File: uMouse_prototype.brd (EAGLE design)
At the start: 90 x 100 mm, 76 parts, among them IC1 LM1117IMPX-5.0, IC2 LM1117IMPX-5.0

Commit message: gotowa, czeka na uwagi Tomka i Kuby
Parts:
- added C27: 100nF 6.3V, rcl:C0805K
- added U$2: (no value), Nordic_nRF:RESC0805_L
- moved 7V4-ON 5.24 mm to (4.45, 57.1), turned to 90 degrees
- moved R1 5.24 mm to (9.53, 57.1), turned to 0 degrees
- moved C6 3.81 mm to (41.9, 73.0)
- moved C7 3.81 mm to (41.9, 76.2)
- moved Q3 2.54 mm to (62.9, 81.3)
- moved C14 1.91 mm to (6.99, 74.9)
- moved C15 1.91 mm to (6.99, 71.8)
- moved IR3 0.38 mm to (60.1, 89.5)
- turned C13 to 90 degrees
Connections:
- removed net AGND: C18.2, C19.2, C20.2, C21.2, C22.2, PT1.K, PT2.K, PT3.K, PT4.K, PT5.K, R19.1, R22.1, U$5.AGND
- removed net N$25: U$5.PA15
- new net N$22: U$2.2, U$5.AVDD
- net 7.4V/VBAT: now also C25.1, C26.1, U$3.5
- net GND: now also C18.2, C19.2, C20.2, C21.2, C22.2, C27.2, PT1.K, PT2.K, PT3.K, PT4.K, PT5.K, R19.1, R22.1, U$5.AGND, U$5.GND_1, U$5.GND_2, U$5.GND_3, U$5.GND_4, U$5.GND_5
- net LEFT-ENC-A: now also JP2.3, U$5.PA0; no longer JP1.1, U$5.PC10
- net LEFT-ENC-B: now also JP2.1, U$5.PA1; no longer JP1.3, U$5.PC12
- net LEFT-M-OUT1: now also JP2.2, U$3.6; no longer JP1.2, U$1.6
- net LEFT-M-OUT2: now also JP2.4, U$3.8; no longer JP1.4, U$1.8
- net LEFT-M-PWM1: now also U$3.3, U$5.PC8; no longer U$1.3, U$5.PB10, U$5.PC6
- net LEFT-M-PWM2: now also U$3.2, U$5.PC6; no longer U$1.2, U$5.PC7
- net RECEIVER_1: now also U$5.PA6; no longer U$5.PA0
- net RECEIVER_2: now also U$5.PA5; no longer U$5.PA1
- net RIGHT-ENC-A: now also JP1.3, U$5.PA9; no longer JP2.1, U$5.PA13
- net RIGHT-ENC-B: now also JP1.1, U$5.PA8; no longer JP2.3, U$5.PA14
- net RIGHT-M-OUT1: now also JP1.2, U$1.6; no longer JP2.2, U$3.6
- net RIGHT-M-OUT2: now also JP1.4, U$1.8; no longer JP2.4, U$3.8
- net RIGHT-M-PWM1: now also U$1.3, U$5.PC9; no longer U$3.3, U$5.PB3, U$5.PC8
- net RIGHT-M-PWM2: now also U$1.2, U$5.PC7; no longer U$3.2, U$5.PB4, U$5.PC9
- net VBAT: no longer C25.1, C26.1, U$3.5
- net VCC: now also C27.1, U$2.1
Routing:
- net VCC: track 0.00 -> 317.8 mm, vias 0 -> 6
- net 7.4V/VBAT: track 0.00 -> 110.1 mm
- net RECEIVER_3: track 0.00 -> 90.9 mm, vias 0 -> 1
- net LEFT-M-PWM1: track 0.00 -> 70.2 mm, vias 0 -> 3
- net LEFT-M-PWM2: track 0.00 -> 68.9 mm, vias 0 -> 3
- net RECEIVER_5: track 0.00 -> 63.3 mm
- net RECEIVER_1: track 0.00 -> 61.4 mm
- net SCL: track 0.00 -> 60.9 mm, vias 0 -> 1
- net SDA: track 0.00 -> 59.6 mm, vias 0 -> 1
- net RECEIVER_4: track 0.00 -> 57.6 mm, vias 0 -> 1
- net RECEIVER_2: track 0.00 -> 56.4 mm
- net RIGHT-M-PWM1: track 0.00 -> 47.9 mm, vias 0 -> 3
- net INT: track 0.00 -> 33.7 mm
- net RIGHT-ENC-B: track 0.00 -> 33.4 mm
- net RIGHT-ENC-A: track 0.00 -> 32.5 mm
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- added copper zone on layer 1, net GND

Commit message: ostatnie poprawki, plytka do enkoderow
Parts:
- added C28: 1uF 16V, rcl:C0805K
- added C29: 4.7uF 6.3V, rcl:C0805K
- added C30: 100nF 6.3V, rcl:C0805K
- added IC3: LM1117IMPX-5.0, lm1117:SOT223
- added JP3, JP4: (no value), pinhead:1X02
- added JP5: (no value), pinhead:1X06
- moved 7V4-ON 5.75 mm to (5.08, 62.9)
- moved R1 5.75 mm to (8.89, 62.9)
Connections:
- new net 5V: C29.1, C30.1, IC3.2, IC3.TAB, JP5.5
- new net EN: JP5.6
- new net RX-STM: JP5.3, U$5.PC5
- new net STATE: JP5.1
- new net TX-STM: JP5.2, U$5.PB10
- net 7.4V/VBAT: now also C28.1, IC3.3
- net GND: now also C28.2, C29.2, C30.2, IC3.1, JP5.4
- net LEFT-M-OUT1: now also JP4.1
- net LEFT-M-OUT2: now also JP4.2
- net RIGHT-M-OUT1: now also JP3.1
- net RIGHT-M-OUT2: now also JP3.2
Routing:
- net LEFT-M-OUT1: track 4.60 -> 45.1 mm, vias 0 -> 1
- net 7.4V/VBAT: track 110.1 -> 143.8 mm, vias 0 -> 2
- net RX-STM: track 0.00 -> 33.0 mm, vias 0 -> 1
- net 5V: track 0.00 -> 26.6 mm, vias 0 -> 2
- net RIGHT-M-OUT2: track 5.24 -> 23.0 mm, vias 0 -> 1
- net RIGHT-M-OUT1: track 5.61 -> 19.8 mm, vias 0 -> 1
- net TX-STM: track 0.00 -> 11.3 mm
- net LEFT-M-OUT2: track 4.60 -> 14.6 mm
- net N$1: track 3.08 -> 1.81 mm
- net INT: vias 0 -> 1

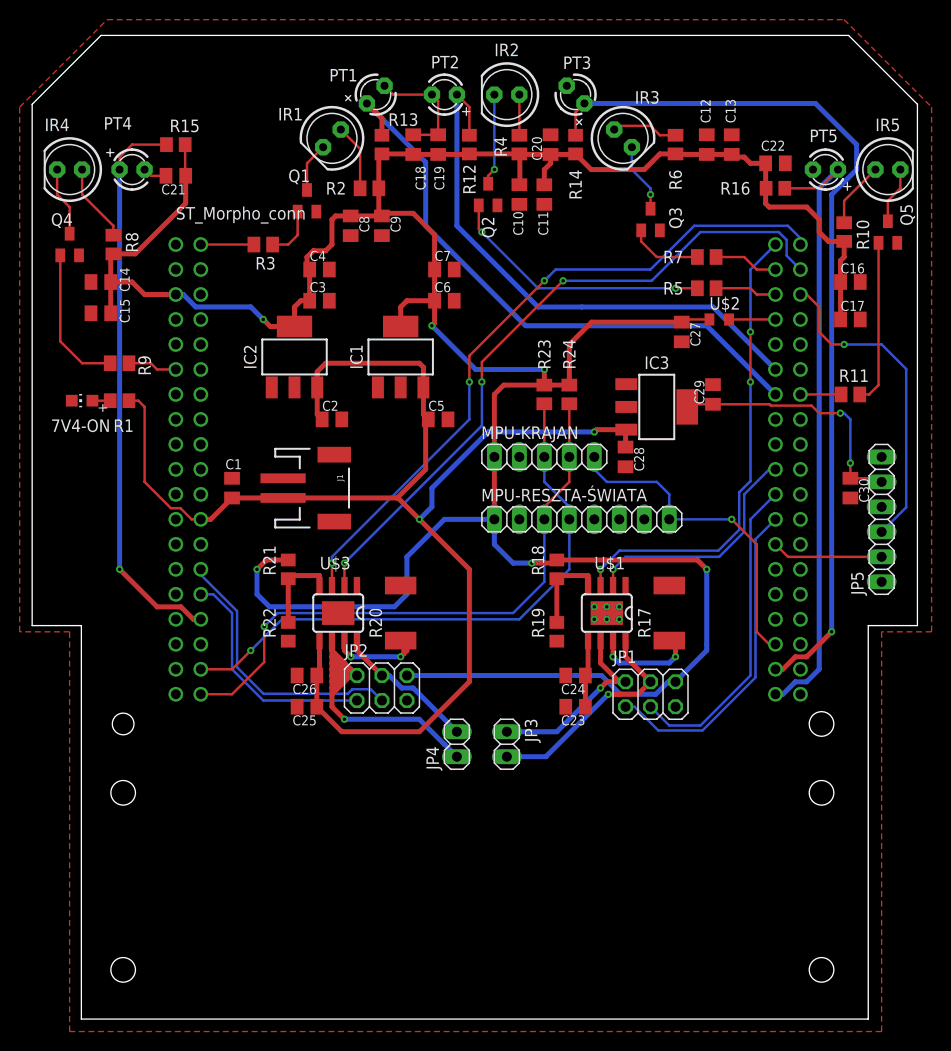
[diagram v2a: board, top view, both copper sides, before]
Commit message: poprawione i2c, dodane otwory pod holderki do ledów IR (tylko przy dwóch)
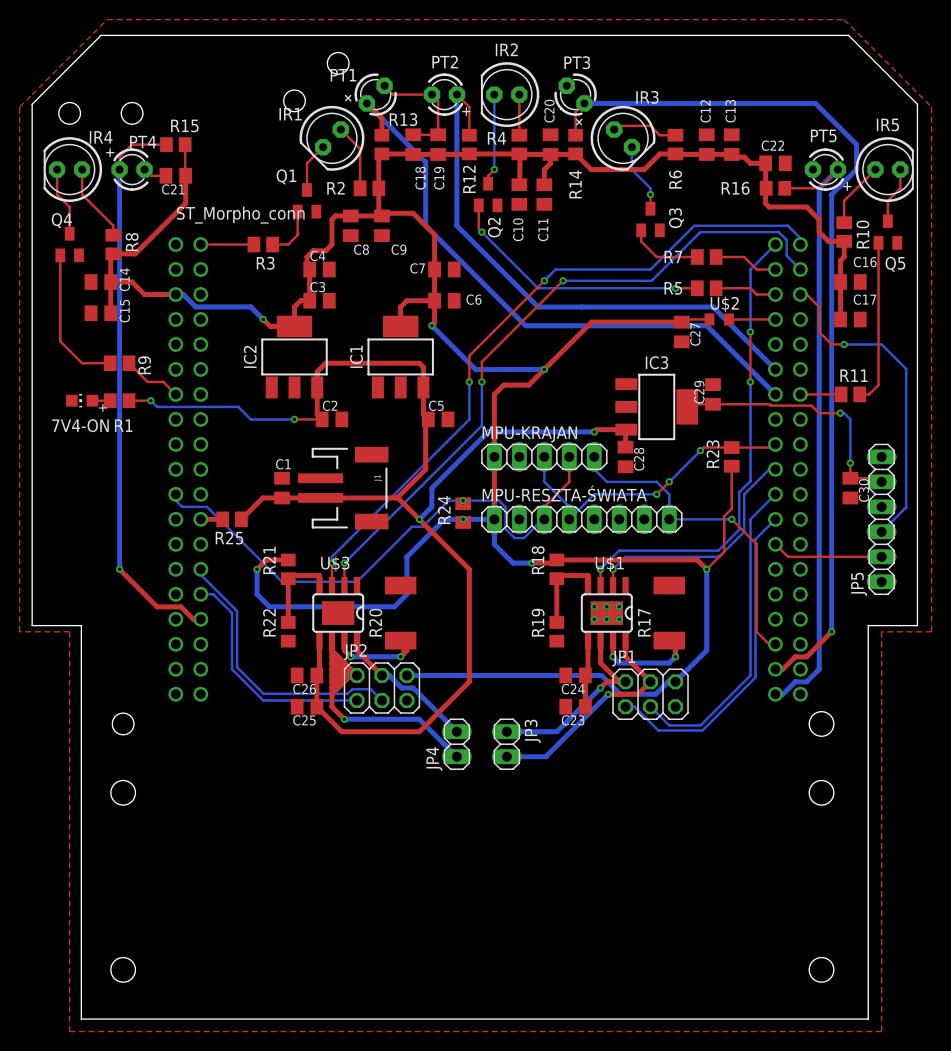
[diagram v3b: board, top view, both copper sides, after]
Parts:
- added R25: 0R, rcl:M0805
- moved R23 20.1 mm to (71.1, 57.1)
- moved R24 16.2 mm to (43.8, 51.4)
- moved C1 5.08 mm to (25.4, 54.0)
- moved J1 3.81 mm to (33.0, 54.0)
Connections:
- new net N$28: R25.2, U$5.VIN
- net 7.4V/VBAT: now also R25.1; no longer U$5.VIN
- net IR4_SIGNAL: now also U$5.PA13; no longer U$5.PF7
- net SCL: now also R24.2, U$5.PB7; no longer R24.1, U$5.PC0
- net SDA: now also R23.2, U$5.PB6; no longer R23.1, U$5.PC1
- net VCC: now also R23.1, R24.1; no longer R23.2, R24.2
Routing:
- net SDA: track 59.6 -> 31.5 mm, vias 1 -> 3
- net VCC: track 317.8 -> 325.7 mm, vias 6 -> 7
- net SCL: track 60.9 -> 56.3 mm
- net N$28: track 0.00 -> 2.23 mm
- net IR4_SIGNAL: track 5.03 -> 6.08 mm
- net 7.4V/VBAT: track 143.8 -> 143.3 mm, vias 2 -> 4
